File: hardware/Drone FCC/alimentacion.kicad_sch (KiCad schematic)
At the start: 14 parts, among them J901 PM02 PixHawk, U901 ZLDO1117QG33TA

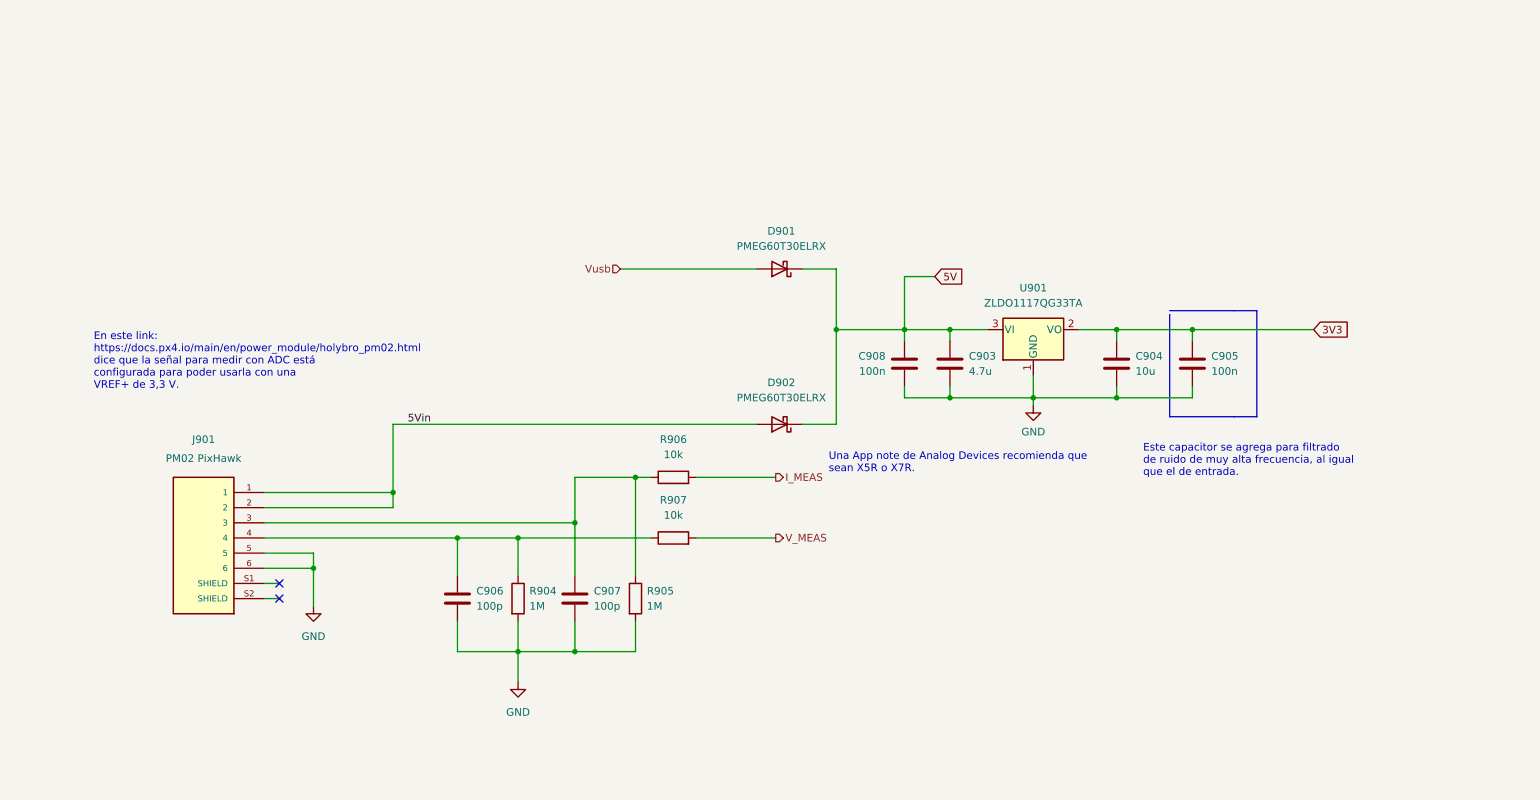
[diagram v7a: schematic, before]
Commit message: re enumeation of componentes
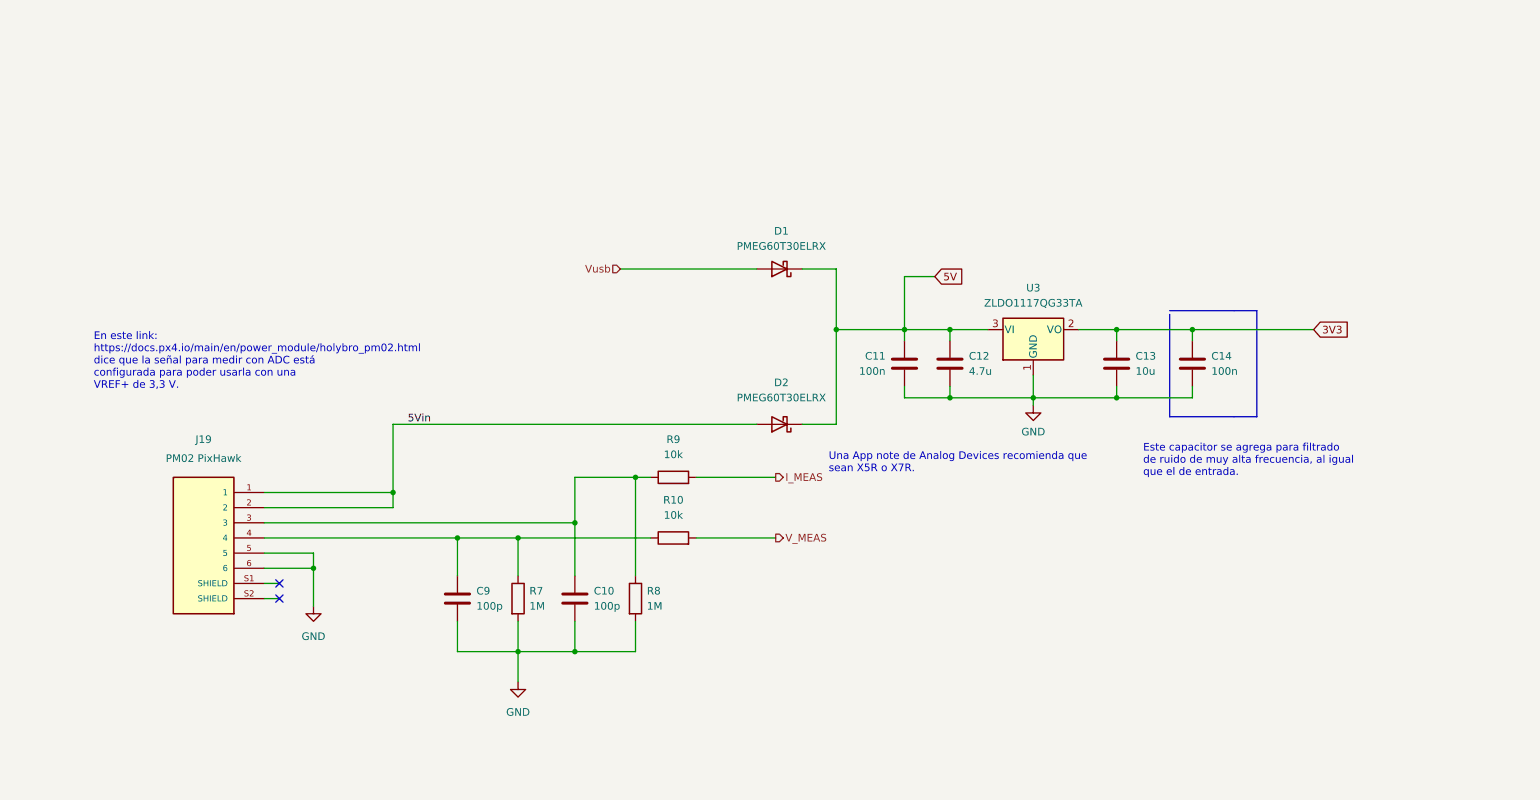
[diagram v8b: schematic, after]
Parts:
- renumbered C907 to C10, C908 to C11, C903 to C12, C904 to C13, C905 to C14, C906 to C9, D901 to D1, D902 to D2, J901 to J19, R907 to R10, R904 to R7, R905 to R8, R906 to R9, U901 to U3
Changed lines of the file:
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@@
   (symbol (lib_id "Device:R") (at 127 100.965 90) (unit 1)
     (in_bom yes) (on_board yes) (fields_autoplaced)
-    (property "Reference" "R907" (id 0) (at 127 94.615 90))
+    (property "Reference" "R10" (id 0) (at 127 94.615 90))
     (property "Value" "10k" (id 1) (at 127 97.155 90))
     (property "Footprint" "Resistor_SMD:R_0402_1005Metric_Pad0.72x0.64mm_HandSolder" (id 2) (at 127 102.743 90)
@@
   (symbol (lib_id "power:GND") (at 100.965 125.095 0) (mirror y) (unit 1)
     (in_bom yes) (on_board yes) (fields_autoplaced)
-    (property "Reference" "#PWR0244" (id 0) (at 100.965 131.445 0)
+    (property "Reference" "#PWR028" (id 0) (at 100.965 131.445 0)
       (effects (font (size 1.27 1.27)) hide)
     )
@@
   (symbol (lib_id "Device:R") (at 120.65 111.125 0) (unit 1)
     (in_bom yes) (on_board yes) (fields_autoplaced)
-    (property "Reference" "R905" (id 0) (at 122.555 109.8549 0)
+    (property "Reference" "R8" (id 0) (at 122.555 109.8549 0)
       (effects (font (size 1.27 1.27)) (justify left))
     )
@@
   (symbol (lib_id "Regulator_Linear:NCP1117-3.3_SOT223") (at 187.325 66.04 0) (unit 1)
     (in_bom yes) (on_board yes) (fields_autoplaced)
-    (property "Reference" "U901" (id 0) (at 187.325 59.055 0))
+    (property "Reference" "U3" (id 0) (at 187.325 59.055 0))
     (property "Value" "ZLDO1117QG33TA" (id 1) (at 187.325 61.595 0))
     (property "Footprint" "Package_TO_SOT_SMD:SOT-223-3_TabPin2" (id 2) (at 187.325 60.96 0)
@@
   (symbol (lib_id "Device:C") (at 173.355 71.755 0) (mirror y) (unit 1)
     (in_bom yes) (on_board yes) (fields_autoplaced)
-    (property "Reference" "C903" (id 0) (at 176.53 70.4849 0)
+    (property "Reference" "C12" (id 0) (at 176.53 70.4849 0)
       (effects (font (size 1.27 1.27)) (justify right))
     )
@@
   (symbol (lib_id "Device:R") (at 100.965 111.125 0) (unit 1)
     (in_bom yes) (on_board yes) (fields_autoplaced)
-    (property "Reference" "R904" (id 0) (at 102.87 109.8549 0)
+    (property "Reference" "R7" (id 0) (at 102.87 109.8549 0)
       (effects (font (size 1.27 1.27)) (justify left))
     )
@@
   (symbol (lib_id "Device:C") (at 90.805 111.125 0) (unit 1)
     (in_bom yes) (on_board yes)
-    (property "Reference" "C906" (id 0) (at 93.98 109.8549 0)
+    (property "Reference" "C9" (id 0) (at 93.98 109.8549 0)
       (effects (font (size 1.27 1.27)) (justify left))
     )
@@
   (symbol (lib_id "Device:D_Schottky") (at 144.78 55.88 180) (unit 1)
     (in_bom yes) (on_board yes) (fields_autoplaced)
-    (property "Reference" "D901" (id 0) (at 145.0975 49.53 0))
+    (property "Reference" "D1" (id 0) (at 145.0975 49.53 0))
     (property "Value" "PMEG60T30ELRX " (id 1) (at 145.0975 52.07 0))
     (property "Footprint" "PMEG60T30ELRX:SODFL3517X110N" (id 2) (at 144.78 55.88 0)
@@
   (symbol (lib_id "Device:C") (at 165.735 71.755 0) (mirror x) (unit 1)
     (in_bom yes) (on_board yes) (fields_autoplaced)
-    (property "Reference" "C908" (id 0) (at 162.56 70.4849 0)
+    (property "Reference" "C11" (id 0) (at 162.56 70.4849 0)
       (effects (font (size 1.27 1.27)) (justify right))
     )
@@
   (symbol (lib_id "Device:C") (at 213.995 71.755 0) (unit 1)
     (in_bom yes) (on_board yes) (fields_autoplaced)
-    (property "Reference" "C905" (id 0) (at 217.17 70.4849 0)
+    (property "Reference" "C14" (id 0) (at 217.17 70.4849 0)
       (effects (font (size 1.27 1.27)) (justify left))
     )
@@
   (symbol (lib_id "Device:R") (at 127 90.805 90) (unit 1)
     (in_bom yes) (on_board yes) (fields_autoplaced)
-    (property "Reference" "R906" (id 0) (at 127 84.455 90))
+    (property "Reference" "R9" (id 0) (at 127 84.455 90))
     (property "Value" "10k" (id 1) (at 127 86.995 90))
     (property "Footprint" "Resistor_SMD:R_0402_1005Metric_Pad0.72x0.64mm_HandSolder" (id 2) (at 127 92.583 90)
@@
   (symbol (lib_id "Device:C") (at 201.295 71.755 0) (unit 1)
     (in_bom yes) (on_board yes) (fields_autoplaced)
-    (property "Reference" "C904" (id 0) (at 204.47 70.4849 0)
+    (property "Reference" "C13" (id 0) (at 204.47 70.4849 0)
       (effects (font (size 1.27 1.27)) (justify left))
     )
@@
   (symbol (lib_id "Device:C") (at 110.49 111.125 0) (unit 1)
     (in_bom yes) (on_board yes) (fields_autoplaced)
-    (property "Reference" "C907" (id 0) (at 113.665 109.8549 0)
+    (property "Reference" "C10" (id 0) (at 113.665 109.8549 0)
       (effects (font (size 1.27 1.27)) (justify left))
     )
@@
   (symbol (lib_id "DF13C-69-1.25v(51):DF13C-6P-1.25V(51)") (at 48.26 103.505 0) (mirror y) (unit 1)
     (in_bom yes) (on_board yes)
-    (property "Reference" "J901" (id 0) (at 48.26 84.455 0))
+    (property "Reference" "J19" (id 0) (at 48.26 84.455 0))
     (property "Value" "PM02 PixHawk" (id 1) (at 48.26 87.63 0))
     (property "Footprint" "DF13C-6P-1.25V(51):HIROSE_DF13C-6P-1.25V(51)" (id 2) (at 48.26 103.505 0)
@@
   (symbol (lib_id "power:GND") (at 187.325 78.74 0) (unit 1)
     (in_bom yes) (on_board yes) (fields_autoplaced)
-    (property "Reference" "#PWR0129" (id 0) (at 187.325 85.09 0)
+    (property "Reference" "#PWR029" (id 0) (at 187.325 85.09 0)
       (effects (font (size 1.27 1.27)) hide)
     )
@@
   (symbol (lib_id "Device:D_Schottky") (at 144.78 81.915 180) (unit 1)
     (in_bom yes) (on_board yes) (fields_autoplaced)
-    (property "Reference" "D902" (id 0) (at 145.0975 74.93 0))
+    (property "Reference" "D2" (id 0) (at 145.0975 74.93 0))
     (property "Value" "PMEG60T30ELRX " (id 1) (at 145.0975 77.47 0))
     (property "Footprint" "PMEG60T30ELRX:SODFL3517X110N" (id 2) (at 144.78 81.915 0)
@@
   (symbol (lib_id "power:GND") (at 66.675 112.395 0) (unit 1)
     (in_bom yes) (on_board yes) (fields_autoplaced)
-    (property "Reference" "#PWR0121" (id 0) (at 66.675 118.745 0)
-      (effects (font (size 1.27 1.27)) hide)
-    )
+    (property "Reference" "#PWR027" (id 0) (at 66.675 118.745 0)
+      (effects (font (size 1.27 1.27)) hide)
+    )
